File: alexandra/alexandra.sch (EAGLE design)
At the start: 16 parts, among them IC1 MEGA8-P, X1 HD44780LCD-1602, X2 22-23-2041

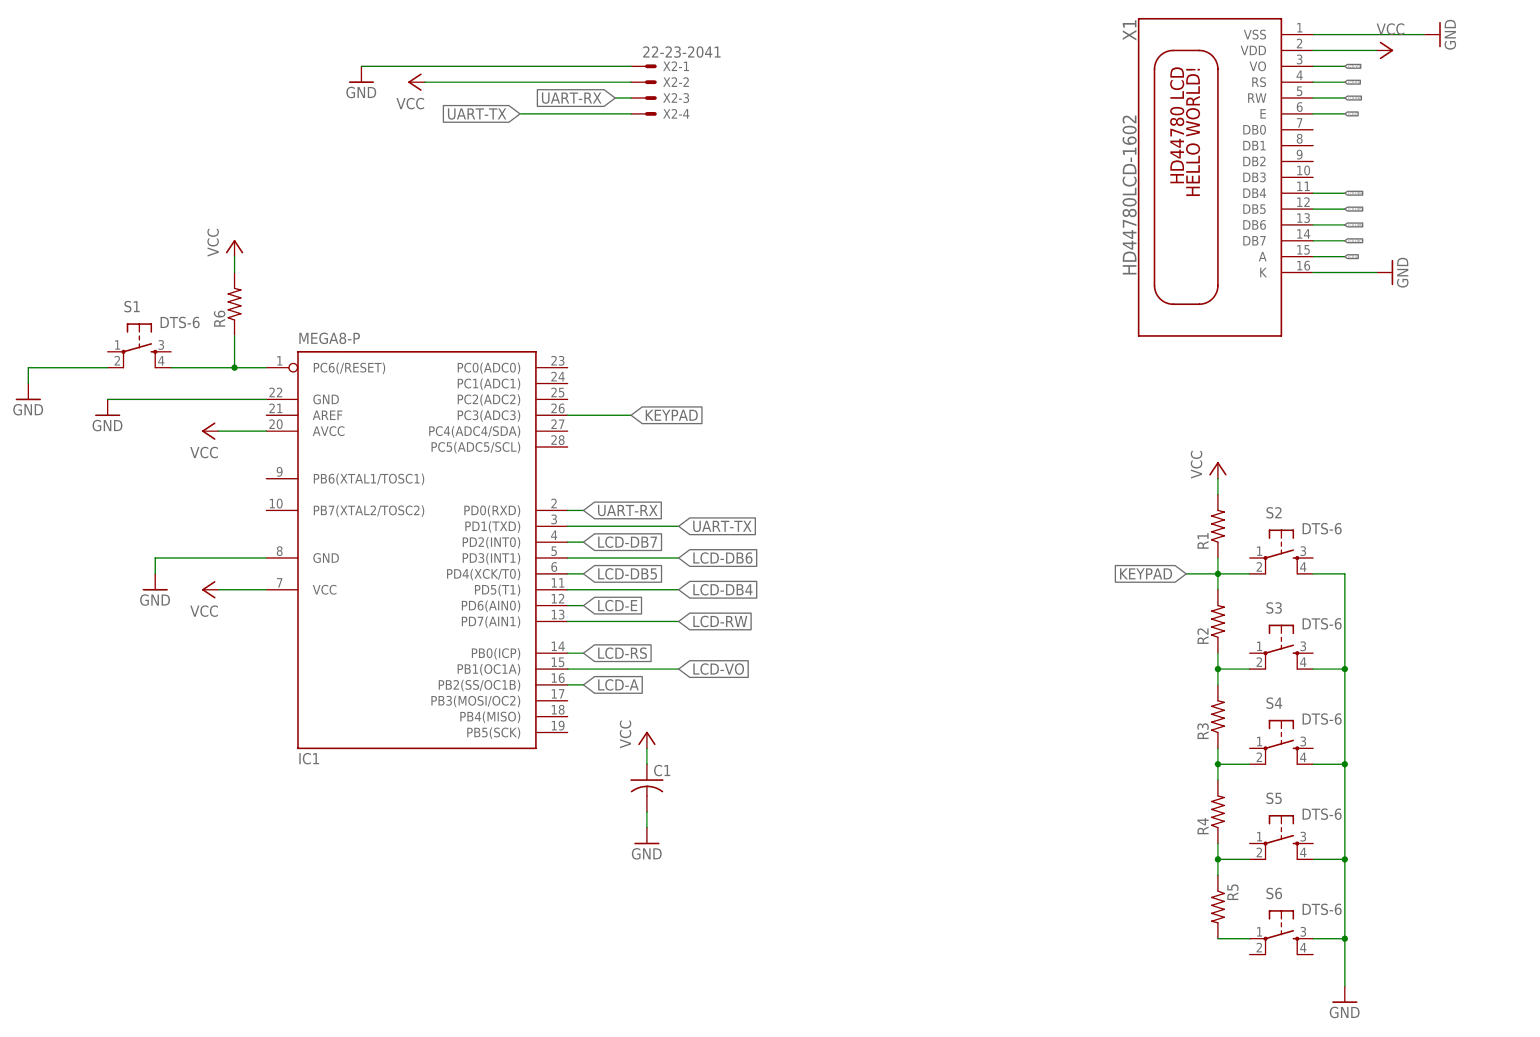
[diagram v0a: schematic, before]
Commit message: Added ISP header, resized labels
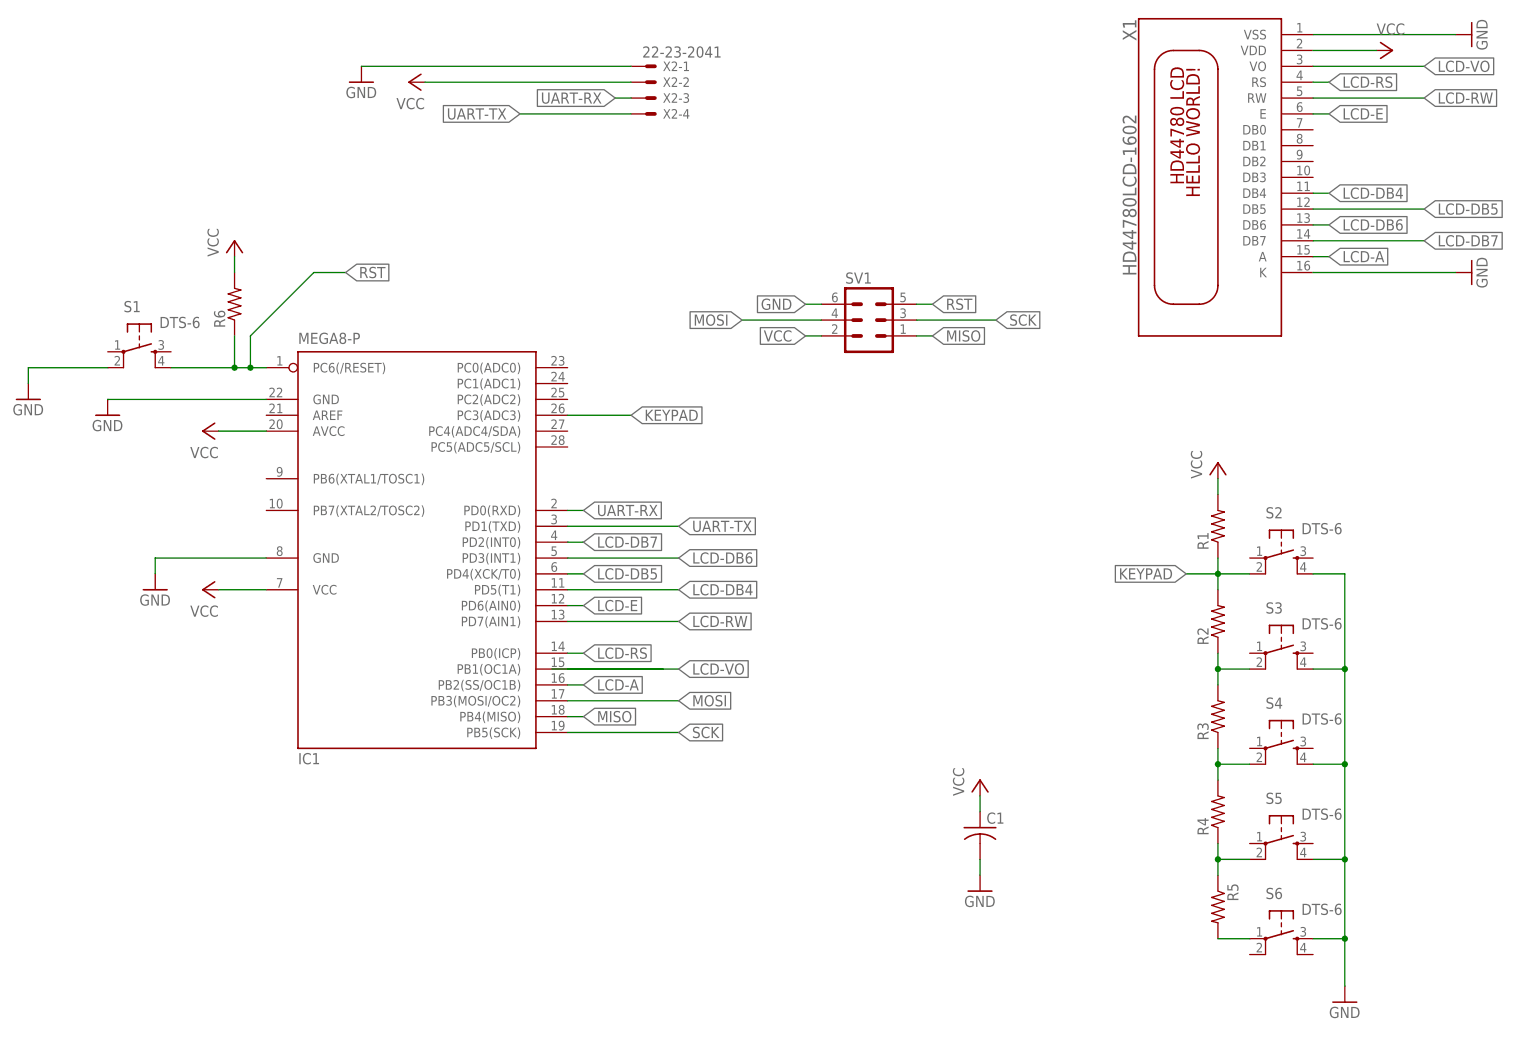
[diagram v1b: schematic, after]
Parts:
- added SV1: (no value), con-lstb:MA03-2
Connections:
- removed net N$1: IC1.PC6(/RESET), R6.1, S1.4
- new net MISO: SV1.1
- new net MOSI: SV1.4
- new net RST: IC1.PC6(/RESET), R6.1, S1.4, SV1.5
- new net SCK: IC1.PB5(SCK), SV1.3
- net GND: now also SV1.6
- net VCC: now also SV1.2
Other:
- moved on the sheet: C1
